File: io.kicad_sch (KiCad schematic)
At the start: 3 parts, among them J2 Header_18x02_2.54mm_2.54mm_St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, J3 Header_18x02_2.54mm_2.54mm_St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, U1 PocketBeagle2

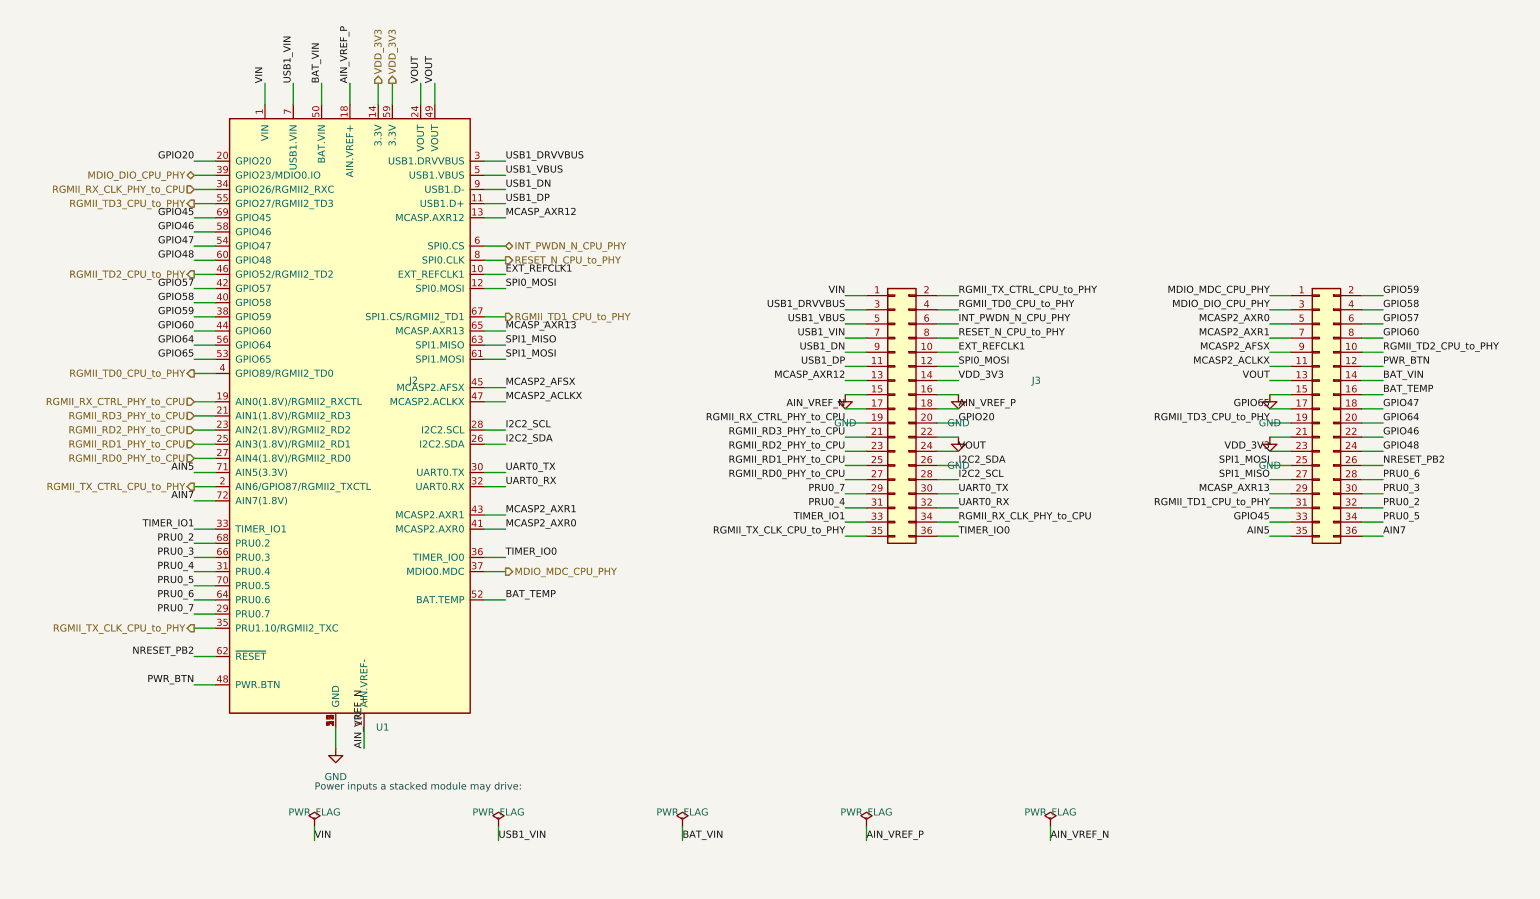
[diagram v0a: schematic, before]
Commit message: Rewire PocketBeagle ground pins and extend signal stubs
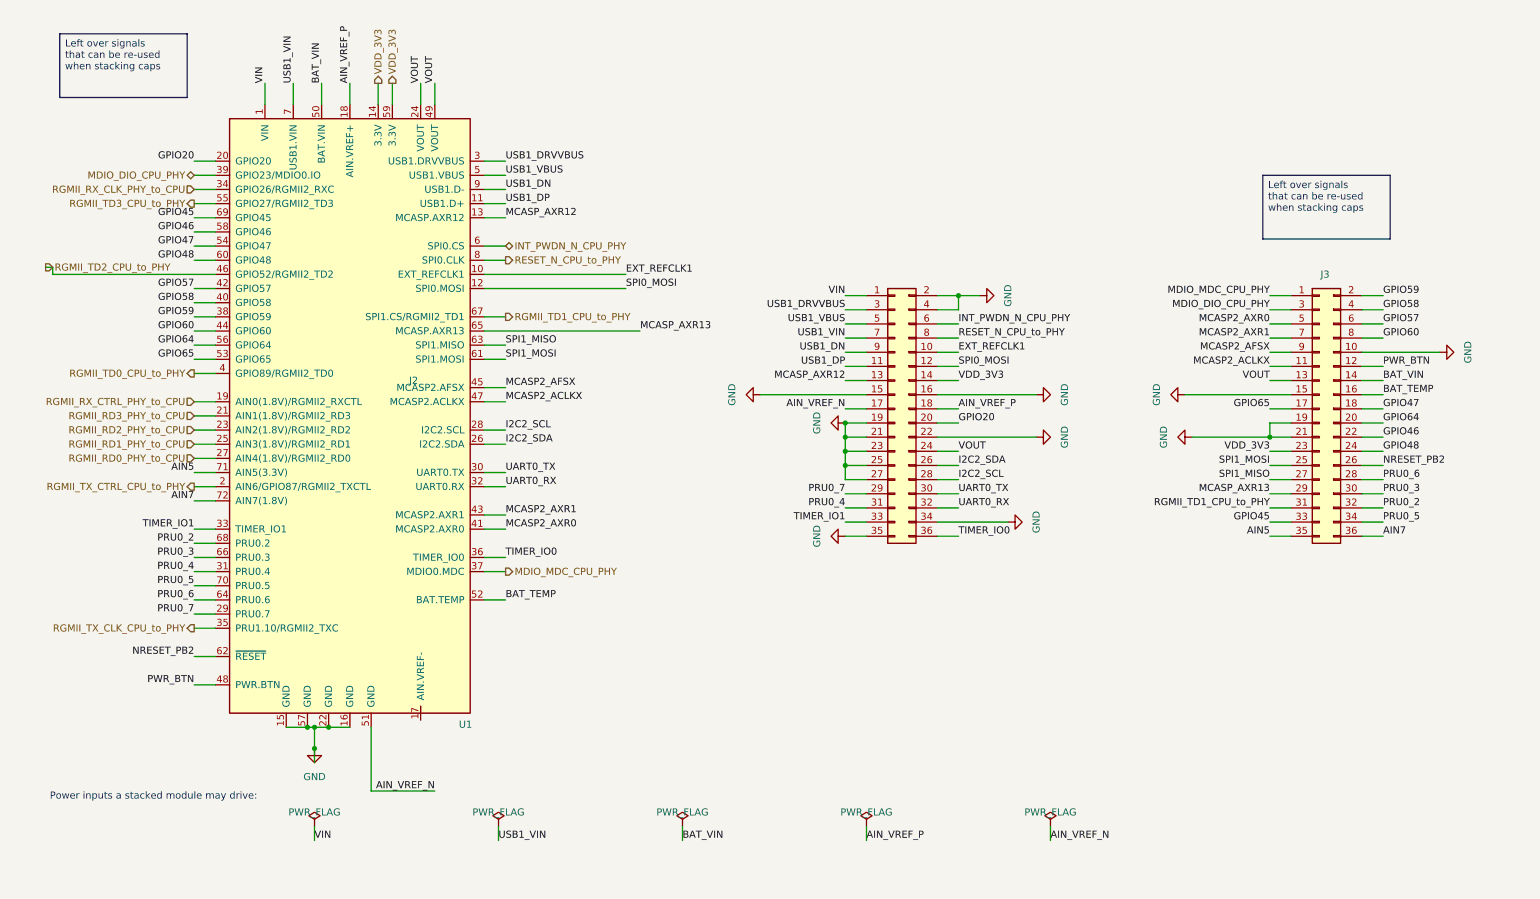
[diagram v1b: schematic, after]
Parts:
- U1: Digikey TBD -> 2820-102110780-ND; LCSC TBD -> NA
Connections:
- net AIN_VREF_N: now also U1.51 (GND); no longer U1.17 (AIN.VREF-)
- net GND: now also J2.19 (Pin_19), J2.2 (Pin_2), J2.21 (Pin_21), J2.23 (Pin_23), J2.25 (Pin_25), J2.27 (Pin_27), J2.34 (Pin_34), J2.35 (Pin_35), J2.4 (Pin_4), J3.10 (Pin_10), J3.19 (Pin_19); no longer U1.51 (GND)
- net RGMII_RD0_PHY_to_CPU: no longer J2.27 (Pin_27)
- net RGMII_RD1_PHY_to_CPU: no longer J2.25 (Pin_25)
- net RGMII_RD2_PHY_to_CPU: no longer J2.23 (Pin_23)
- net RGMII_RD3_PHY_to_CPU: no longer J2.21 (Pin_21)
- net RGMII_RX_CLK_PHY_to_CPU: no longer J2.34 (Pin_34)
- net RGMII_RX_CTRL_PHY_to_CPU: no longer J2.19 (Pin_19)
- net RGMII_TD0_CPU_to_PHY: no longer J2.4 (Pin_4)
- net RGMII_TD2_CPU_to_PHY: no longer J3.10 (Pin_10)
- net RGMII_TD3_CPU_to_PHY: no longer J3.19 (Pin_19)
- net RGMII_TX_CLK_CPU_to_PHY: no longer J2.35 (Pin_35)
- net RGMII_TX_CTRL_CPU_to_PHY: no longer J2.2 (Pin_2)
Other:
- company: (none) -> Kebag Logic: kebag-logic.com
- title: (none) -> I/O

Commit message: Updating to KiCad 10 + updsate the library
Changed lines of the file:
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@@
 	(text "Power inputs a stacked module may drive:"
 		(exclude_from_sim no)
-		(at 13.462 151.638 0)
+		(at 13.208 166.878 0)
 		(effects
 			(font
@@
 	(text_box "Left over signals that can be re-used when stacking caps"
 		(exclude_from_sim no)
-		(at 231.14 39.37 0)
-		(size 22.86 11.43)
+		(at 161.29 20.32 0)
+		(size 22.86 13.97)
 		(margins 0.9525 0.9525 0.9525 0.9525)
 		(stroke

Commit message: Fix J2/J3 pass-through nets, AIN_VREF_N and U1 symbol
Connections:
- net AIN_VREF_N: now also U1.17 (AIN.VREF-); no longer U1.51 (GND)
- net GND: now also U1.51 (GND); no longer J2.19 (Pin_19), J2.2 (Pin_2), J2.21 (Pin_21), J2.23 (Pin_23), J2.25 (Pin_25), J2.27 (Pin_27), J2.34 (Pin_34), J2.35 (Pin_35), J2.4 (Pin_4), J3.10 (Pin_10), J3.19 (Pin_19)
- net RGMII_RD0_PHY_to_CPU: now also J2.27 (Pin_27)
- net RGMII_RD1_PHY_to_CPU: now also J2.25 (Pin_25)
- net RGMII_RD2_PHY_to_CPU: now also J2.23 (Pin_23)
- net RGMII_RD3_PHY_to_CPU: now also J2.21 (Pin_21)
- net RGMII_RX_CLK_PHY_to_CPU: now also J2.34 (Pin_34)
- net RGMII_RX_CTRL_PHY_to_CPU: now also J2.19 (Pin_19)
- net RGMII_TD0_CPU_to_PHY: now also J2.4 (Pin_4)
- net RGMII_TD2_CPU_to_PHY: now also J3.10 (Pin_10)
- net RGMII_TD3_CPU_to_PHY: now also J3.19 (Pin_19)
- net RGMII_TX_CLK_CPU_to_PHY: now also J2.35 (Pin_35)
- net RGMII_TX_CTRL_CPU_to_PHY: now also J2.2 (Pin_2)

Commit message: Switch BOM to in-stock LCSC parts, U3 to TLV73311
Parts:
- J2, J3: Digikey TBD -> (none); LCSC TBD -> C41376109; MPN BHR-36-VUA -> HC-PZ254-11.5L-2x18PZ; Mouser 737-BHR-36-VUA -> (none)
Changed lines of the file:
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@@
 			)
 		)
-		(property "Datasheet" "https://app.adam-tech.com/products/download/data_sheet/203218/bhr-xx-v"
+		(property "Datasheet" "https://www.lcsc.com/datasheet/lcsc_datasheet_2408301436_Hong-Cheng-HC-PZ254-11-5L-2x18PZ_C41376109.pdf"
 			(at 78.74 78.74 0)
 			(hide yes)
@@
 			)
 		)
-		(property "MPN" "BHR-36-VUA"
+		(property "MPN" "HC-PZ254-11.5L-2x18PZ"
 			(at 78.74 78.74 0)
 			(hide yes)
@@
 			)
 		)
-		(property "Mouser" "737-BHR-36-VUA"
+		(property "Mouser" ""
 			(at 78.74 78.74 0)
 			(hide yes)
@@
 			)
 		)
-		(property "Digikey" "TBD"
+		(property "Digikey" ""
 			(at 78.74 78.74 0)
 			(hide yes)
@@
 			)
 		)
-		(property "LCSC" "TBD"
+		(property "LCSC" "C41376109"
 			(at 78.74 78.74 0)
 			(hide yes)
@@
 			)
 		)
-		(property "Datasheet" "https://app.adam-tech.com/products/download/data_sheet/203218/bhr-xx-v"
+		(property "Datasheet" "https://www.lcsc.com/datasheet/lcsc_datasheet_2408301436_Hong-Cheng-HC-PZ254-11-5L-2x18PZ_C41376109.pdf"
 			(at 190.5 78.74 0)
 			(hide yes)
@@
 			)
 		)
-		(property "MPN" "BHR-36-VUA"
-			(at 190.5 78.74 0)
-			(hide yes)
-			(show_name no)
-			(do_not_autoplace no)
-			(effects
-				(font
-					(size 1.27 1.27)
-				)
-			)
-		)
-		(property "Mouser" "737-BHR-36-VUA"
-			(at 190.5 78.74 0)
-			(hide yes)
-			(show_name no)
-			(do_not_autoplace no)
-			(effects
-				(font
-					(size 1.27 1.27)
-				)
-			)
-		)
-		(property "Digikey" "TBD"
-			(at 190.5 78.74 0)
-			(hide yes)
-			(show_name no)
-			(do_not_autoplace no)
-			(effects
-				(font
-					(size 1.27 1.27)
-				)
-			)
-		)
-		(property "LCSC" "TBD"
-			(at 190.5 78.74 0)
-			(hide yes)
+		(property "MPN" "HC-PZ254-11.5L-2x18PZ"
+			(at 190.5 78.74 0)
+			(hide yes)
+			(show_name no)
+			(do_not_autoplace no)
+			(effects
+				(font
+					(size 1.27 1.27)
+				)
+			)
+		)
+		(property "Mouser" ""
+			(at 190.5 78.74 0)
+			(hide yes)
+			(show_name no)
+			(do_not_autoplace no)
+			(effects
+				(font
+					(size 1.27 1.27)
+				)
+			)
+		)
+		(property "Digikey" ""
+			(at 190.5 78.74 0)
+			(hide yes)
+			(show_name no)
+			(do_not_autoplace no)
+			(effects
+				(font
+					(size 1.27 1.27)
+				)
+			)
+		)
+		(property "LCSC" "C41376109"
+			(at 190.5 78.74 0)
+			(hide yes)
